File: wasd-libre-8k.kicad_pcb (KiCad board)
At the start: 2 copper layers, 100 x 40 mm, 63 parts, among them J1 Conn_01x05, J2 USB_C_Receptacle_USB2.0, J3 Conn_01x07, J32 Conn_01x32, U1 MX25R3235FM1xx1, U2 ICE40HX1K-TQ144, U20 ICE40HX8K-BG121, U3 NCV8114ASN120T1G, U4 NCV8114ASN330T1G, U5 NCV8114ASN180T1G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

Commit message: Some USB changes
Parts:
- removed G***: LOGO, wasd-libre-8k:logo
- removed G***: LOGO, wasd-libre-8k:forksand
- added D10: PGB1010603NRHF, Diode_SMD:D_0603_1608Metric, B.Cu at (134.5, 79.8)
- added D11: PGB1010603NRHF, Diode_SMD:D_0603_1608Metric, B.Cu at (138.0, 79.8)
- added R90: 5K1, Resistor_SMD:R_0402_1005Metric, B.Cu at (133.8, 78.4)
- added R91: 5K1, Resistor_SMD:R_0402_1005Metric, B.Cu at (138.7, 78.4)
- added R92: 22, Resistor_SMD:R_0402_1005Metric, B.Cu at (135.3, 77.0)
- added R93: 22, Resistor_SMD:R_0402_1005Metric, B.Cu at (137.2, 77.0)
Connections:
- J2 pad A5: (no net) -> Net-(J2-PadA5)
- J2 pad A6: (no net) -> /D+
- J2 pad A7: (no net) -> /D-
- J2 pad B5: (no net) -> Net-(J2-PadB5)
- J2 pad B6: (no net) -> /D+
- J2 pad B7: (no net) -> /D-
- U2 pad 128: (no net) -> /USB_D-
- U2 pad 129: (no net) -> /USB_D+
- U20 pad E1: (no net) -> /USB_D-
- U20 pad F1: (no net) -> /USB_D+
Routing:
- net /USB_D+: track 0.00 -> 74.1 mm, vias 0 -> 4
- net /USB_D-: track 0.00 -> 73.2 mm, vias 0 -> 4
- net GND: track 107.8 -> 116.3 mm
- net /D+: track 0.00 -> 5.70 mm
- net /D-: track 0.00 -> 5.47 mm, vias 0 -> 2
- net Net-(J2-PadA5): track 0.00 -> 4.40 mm
- net Net-(J2-PadB5): track 0.00 -> 4.15 mm

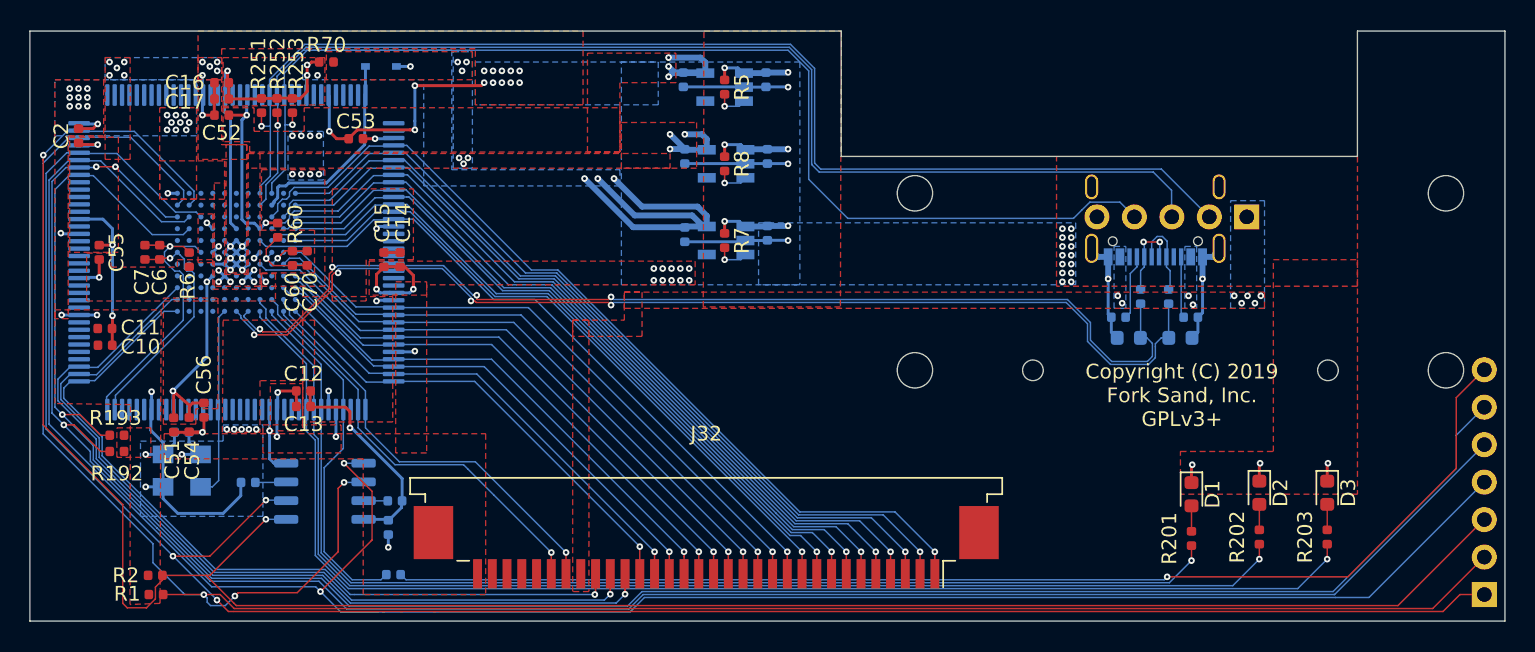
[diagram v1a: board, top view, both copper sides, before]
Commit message: Fix mechanical dimensions, adding spare lines
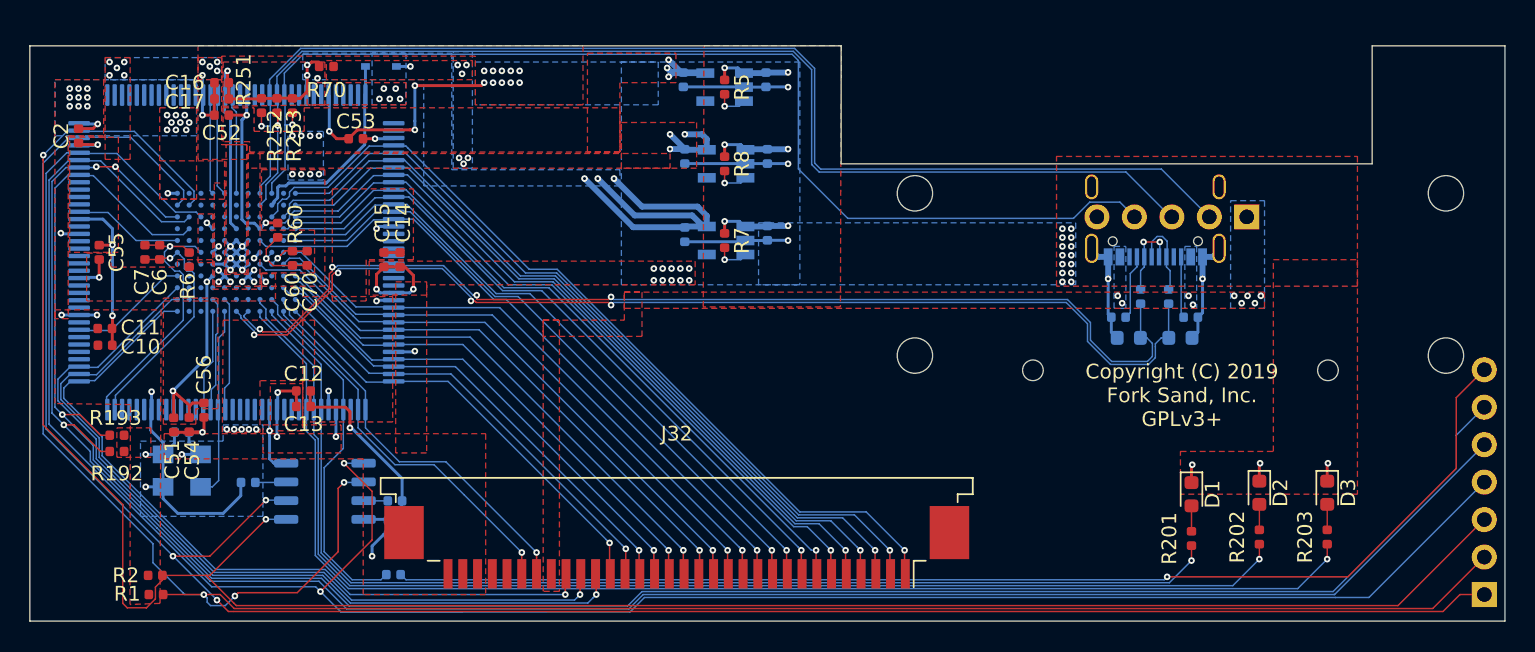
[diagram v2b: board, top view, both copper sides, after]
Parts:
- moved J32 2.00 mm to (103.8, 94.0)
- moved R70 0.30 mm to (80.1, 61.4)
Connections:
- U2 pad 20: (no net) -> /SPR3
- U2 pad 22: (no net) -> /SPR2
- U2 pad 23: (no net) -> /SPR1
- U2 pad 44: (no net) -> /SPR4
- U2 pad 60: (no net) -> /SPR5
- U2 pad 87: (no net) -> /SPR6
- U2 pad 88: (no net) -> /SPR7
- U2 pad 90: (no net) -> /SPR8
- U20 pad F11: (no net) -> /SPR8
- U20 pad G11: (no net) -> /SPR7
- U20 pad G2: (no net) -> /SPR3
- U20 pad H1: (no net) -> /SPR1
- U20 pad H11: (no net) -> /SPR6
- U20 pad H2: (no net) -> /SPR2
- U20 pad L4: (no net) -> /SPR4
- U20 pad L7: (no net) -> /SPR5
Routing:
- net /SPR4: track 0.00 -> 8.23 mm
- net /SPR3: track 0.00 -> 7.77 mm
- net /SPR2: track 0.00 -> 7.71 mm
- net /SPR5: track 0.00 -> 7.49 mm
- net /SPR1: track 0.00 -> 6.95 mm
- net /SPR7: track 0.00 -> 6.91 mm
- net /SPR8: track 0.00 -> 6.82 mm
- net /SPR6: track 0.00 -> 6.78 mm
- net /COL7: track 53.6 -> 51.5 mm
- net /COL2: track 35.2 -> 33.1 mm
- net /RGB_OUT: track 28.0 -> 26.0 mm
- net /ROW0: track 60.3 -> 58.3 mm
- net /COL0: track 37.5 -> 35.5 mm
- net /COL6: track 56.2 -> 54.2 mm
- net /PWM_OUT: track 29.5 -> 27.5 mm
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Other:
- board size 100 x 40 mm -> 100 x 39 mm

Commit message: Silkscreen sign for prog port
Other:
- board text added: "DBG"
- board text added: "DONE"
- board text added: "MISO"
- board text added: "MOSI"
- board text added: "RST"
- board text added: "SCK"
- board text added: "SS"
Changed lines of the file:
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@@
   (general
     (thickness 1.6)
-    (drawings 16)
+    (drawings 23)
     (tracks 1233)
     (zones 0)
@@
     )
   )
+  (gr_text MISO (at 153.3 97.2) (layer F.SilkS)
+    (effects (font (size 1 1) (thickness 0.2)))
+  )
+  (gr_text SCK (at 153 94.8) (layer F.SilkS)
+    (effects (font (size 1 1) (thickness 0.2)))
+  )
+  (gr_text SS (at 152.4 92.4) (layer F.SilkS)
+    (effects (font (size 1 1) (thickness 0.2)))
+  )
+  (gr_text MOSI (at 153.3 89.7) (layer F.SilkS)
+    (effects (font (size 1 1) (thickness 0.2)))
+  )
+  (gr_text RST (at 152.8 87.2) (layer F.SilkS)
+    (effects (font (size 1 1) (thickness 0.2)))
+  )
+  (gr_text DONE (at 153.4 84.6) (layer F.SilkS)
+    (effects (font (size 1 1) (thickness 0.2)))
+  )
+  (gr_text DBG (at 152.9 82) (layer F.SilkS)
+    (effects (font (size 1 1) (thickness 0.2)))
+  )
   (gr_circle (center 156 81) (end 157.2 81) (layer Edge.Cuts) (width 0.05))
   (gr_circle (center 120 81) (end 121.2 81) (layer Edge.Cuts) (width 0.05))
@@
   (gr_circle (center 156 70) (end 157.2 70) (layer Edge.Cuts) (width 0.05))
   (gr_circle (center 120 70) (end 121.2 70) (layer Edge.Cuts) (width 0.05))
-  (via (at 84.4 63.6) (size 0.45) (drill 0.2) (layers F.Cu B.Cu) (net 55))
-  (via (at 83.7 63.6) (size 0.45) (drill 0.2) (layers F.Cu B.Cu) (net 55))
-  (via (at 84 62.9) (size 0.45) (drill 0.2) (layers F.Cu B.Cu) (net 55))
-  (via (at 84.8 62.9) (size 0.45) (drill 0.2) (layers F.Cu B.Cu) (net 55))
-  (via (at 85.1 63.6) (size 0.45) (drill 0.2) (layers F.Cu B.Cu) (net 55))
-  (via (at 96.3 97.2) (size 0.45) (drill 0.2) (layers F.Cu B.Cu) (net 47))
   (via (at 91.4 62.5) (size 0.45) (drill 0.2) (layers F.Cu B.Cu) (net 1))
   (via (at 92 61.7) (size 0.45) (drill 0.2) (layers F.Cu B.Cu) (net 1))
@@
   (segment (start 64.69999 87.89999) (end 72.5 95.7) (width 0.1) (layer B.Cu) (net 46))
   (segment (start 97.299996 97.2) (end 97.299996 95.800004) (width 0.1) (layer F.Cu) (net 46))
+  (via (at 96.3 97.2) (size 0.45) (drill 0.2) (layers F.Cu B.Cu) (net 47))
   (segment (start 70 78) (end 69.1 78) (width 0.1) (layer B.Cu) (net 47))
   (segment (start 69.1 78) (end 64.4 82.7) (width 0.1) (layer B.Cu) (net 47))
@@
   (segment (start 72.8 79.8) (end 73.2 79.4) (width 0.1) (layer B.Cu) (net 54))
   (segment (start 73.2 79.4) (end 73.2 78) (width 0.1) (layer B.Cu) (net 54))
+  (via (at 84.4 63.6) (size 0.45) (drill 0.2) (layers F.Cu B.Cu) (net 55))
+  (via (at 83.7 63.6) (size 0.45) (drill 0.2) (layers F.Cu B.Cu) (net 55))
+  (via (at 84 62.9) (size 0.45) (drill 0.2) (layers F.Cu B.Cu) (net 55))
+  (via (at 84.8 62.9) (size 0.45) (drill 0.2) (layers F.Cu B.Cu) (net 55))
+  (via (at 85.1 63.6) (size 0.45) (drill 0.2) (layers F.Cu B.Cu) (net 55))
   (via (at 79.5 62.2) (size 0.45) (drill 0.2) (layers F.Cu B.Cu) (net 55))
   (via (at 78.8 61.3) (size 0.45) (drill 0.2) (layers F.Cu B.Cu) (net 55))

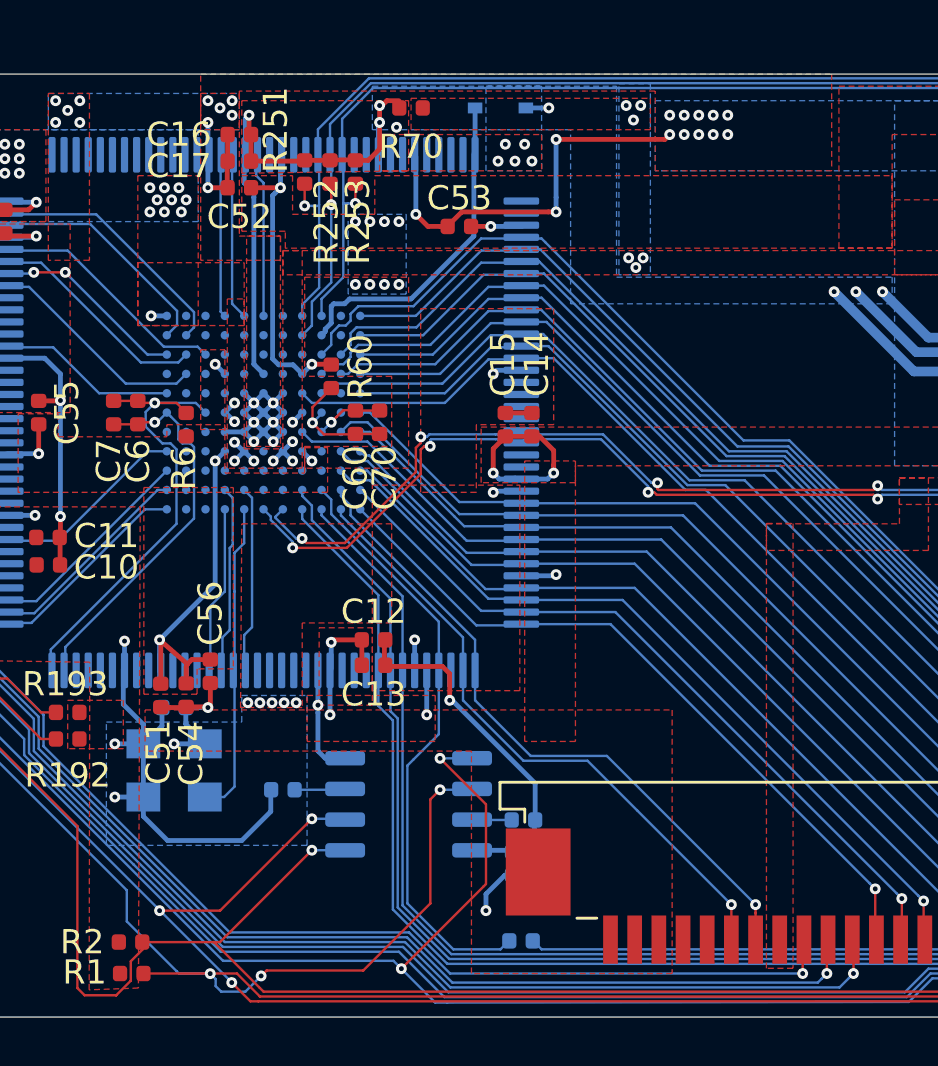
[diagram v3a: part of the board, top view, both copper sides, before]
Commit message: RGB LED level converter added
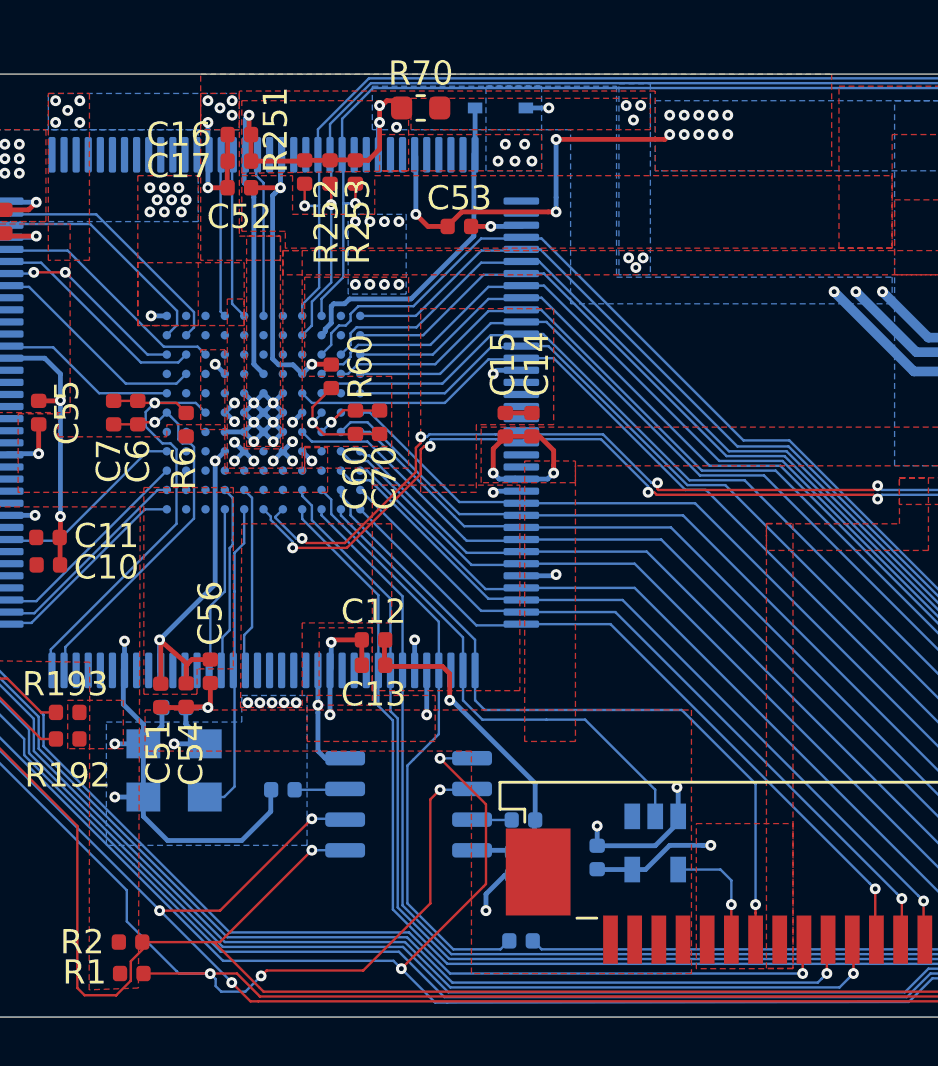
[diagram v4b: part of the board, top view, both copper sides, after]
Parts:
- added C20: 0.1 uF, Capacitor_SMD:C_0402_1005Metric, B.Cu at (87.8, 92.4)
- added U6: SN74LVC1G14DBV, Package_TO_SOT_SMD:SOT-23-5, B.Cu at (90.2, 91.8)
- R70: footprint Resistor_SMD:R_0402_1005Metric -> Resistor_SMD:R_0603_1608Metric
- moved R70 0.40 mm to (80.5, 61.4)
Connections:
- J32 pad 28: (no net) -> +5V
- J32 pad 31: (no net) -> GND
- U2 pad 2: /RGB_OUT -> /RGB_DRV
- U20 pad B1: /RGB_OUT -> /RGB_DRV
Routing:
- net /RGB_OUT: track 26.0 -> 4.79 mm
- net /RGB_DRV: track 0.00 -> 20.6 mm
- net GND: track 117.5 -> 123.5 mm, vias 75 -> 77
- net +5V: track 15.9 -> 21.0 mm, vias 15 -> 16
- net /PWM_OUT: track 27.5 -> 30.5 mm

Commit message: J32 (32 pins) replaced by 30 pins for using TE connector
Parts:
- J32: value Conn_01x32 -> Conn_01x30; footprint wasd-libre-8k:Noname_1x32-1MP_P1.0mm_Horizontal -> Connector_FFC-FPC:TE_3-84953-0_1x30-1MP_P1.0mm_Horizontal
- moved J32 1.00 mm to (104.8, 94.0)
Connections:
- J32 pad 29: (no net) -> GND
- J32 pad 30: (no net) -> GND

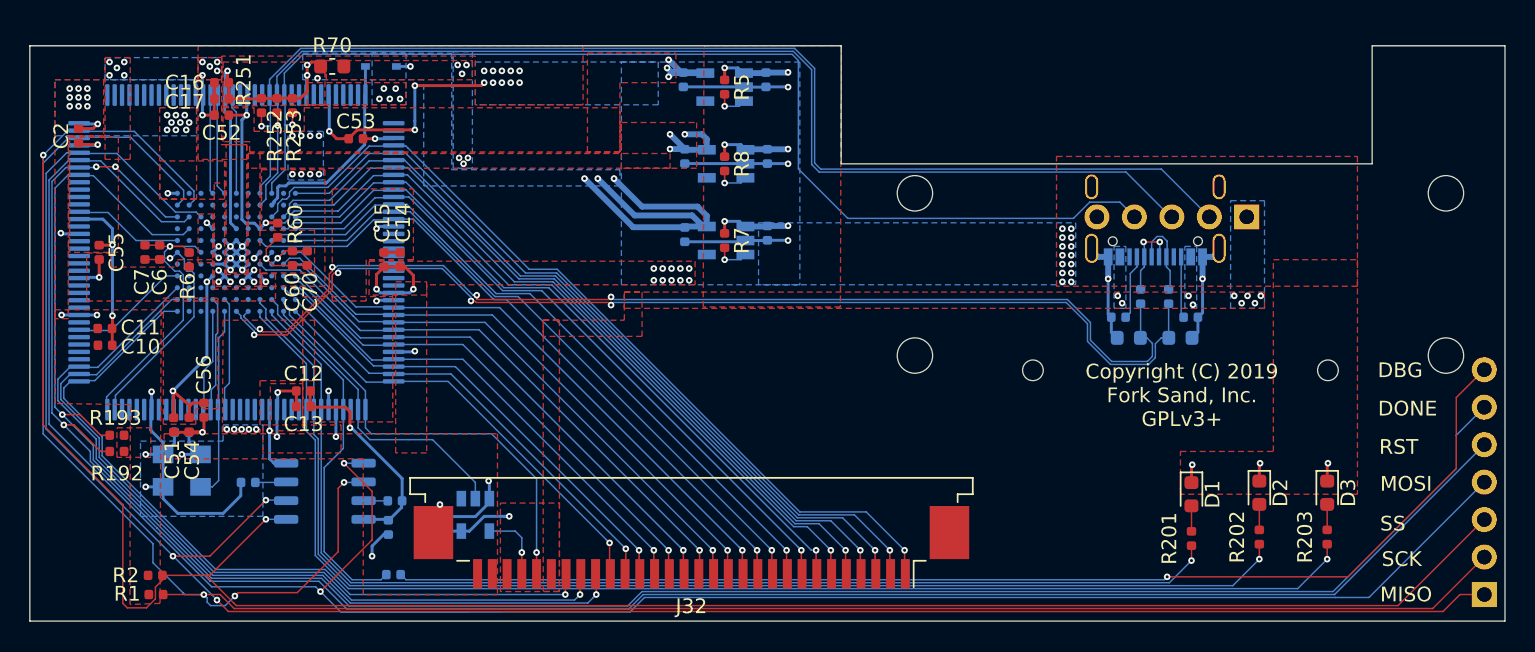
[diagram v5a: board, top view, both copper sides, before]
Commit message: Adding some silkscreen, moved I2C lines, added additional holes for USB
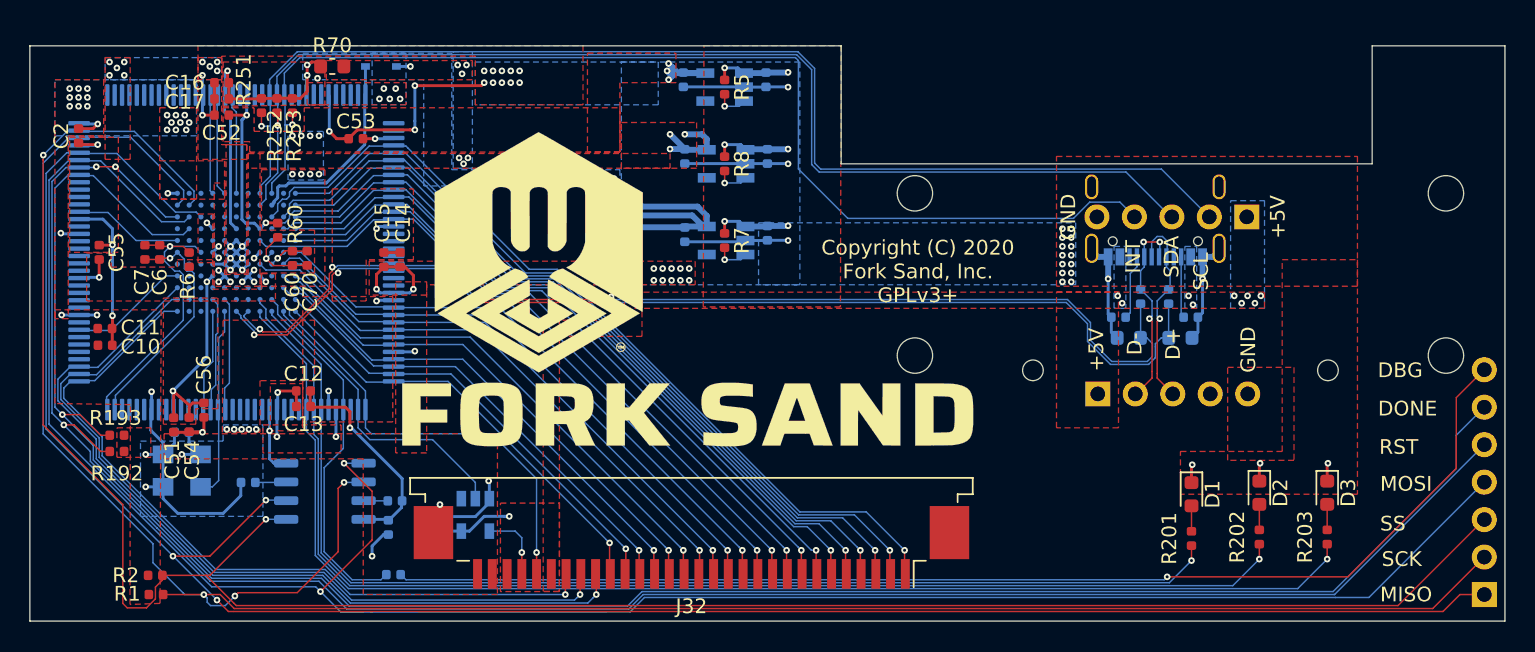
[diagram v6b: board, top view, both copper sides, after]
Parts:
- added G***: LOGO, wasd-libre-8k:logo, F.Cu at (94.5, 74.1)
- added G***: LOGO, wasd-libre-8k:forksand, F.Cu at (104.6, 85.0)
- added J12: Conn_01x05, Connector_PinHeader_2.54mm:PinHeader_1x05_P2.54mm_Vertical, B.Cu at (132.4, 83.6)
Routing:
- net /D-: track 5.47 -> 13.5 mm, vias 2 -> 3
- net /D+: track 5.70 -> 13.7 mm, vias 0 -> 1
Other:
- board text added: "+5V"
- board text added: "Copyright (C) 2020 Fork Sand, Inc. GPLv3+"
- board text added: "D+"
- board text added: "D-"
- board text added: "GND"
- board text added: "INT"
- board text added: "SCL"
- board text added: "SDA"
- board text removed: "Copyright (C) 2019 Fork Sand, Inc. GPLv3+"
